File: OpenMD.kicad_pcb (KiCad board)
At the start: 4 copper layers, 80 x 50 mm, 167 parts, among them IC2 RAA211, J1 GND, J2 Digital, J3 Analog, J4 Sensors, J5 A, J6 B, J7 C, J8 V_{BATT}, Q1 EPC2065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

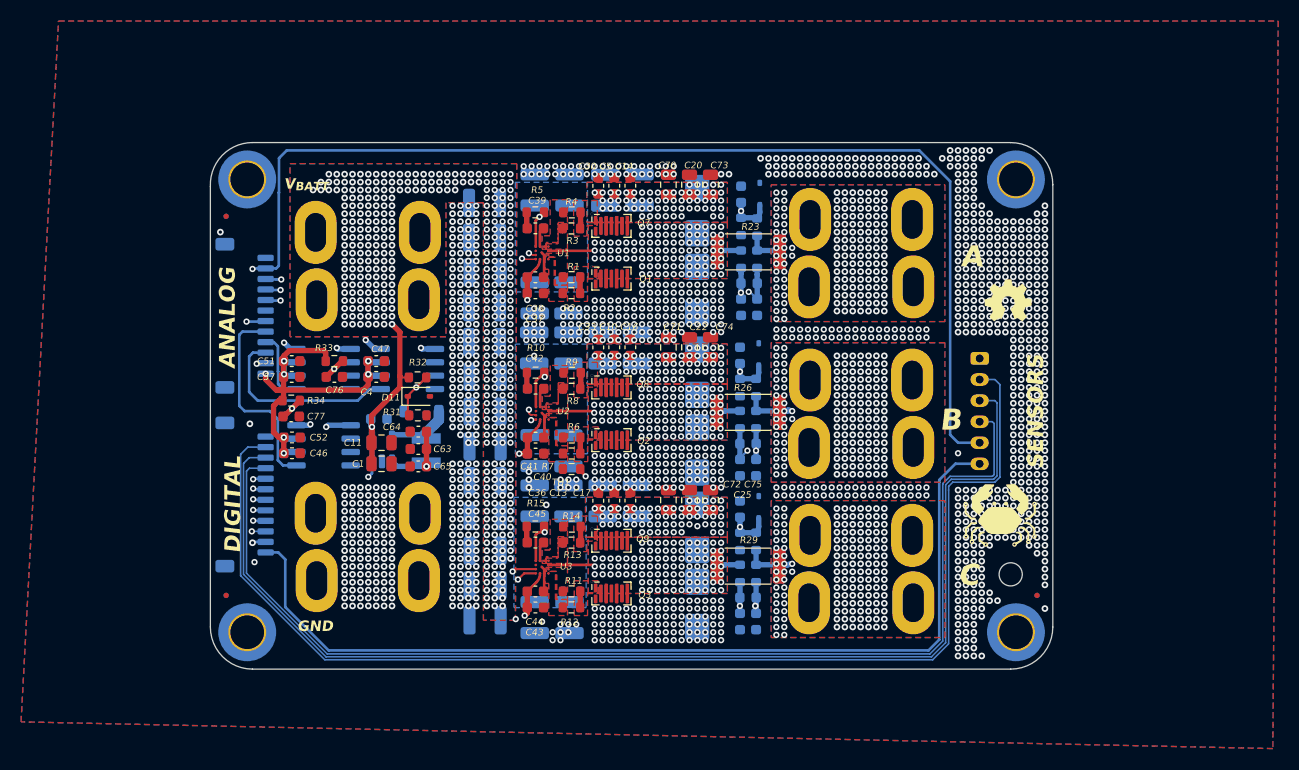
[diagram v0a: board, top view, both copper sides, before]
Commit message: added ESD protection
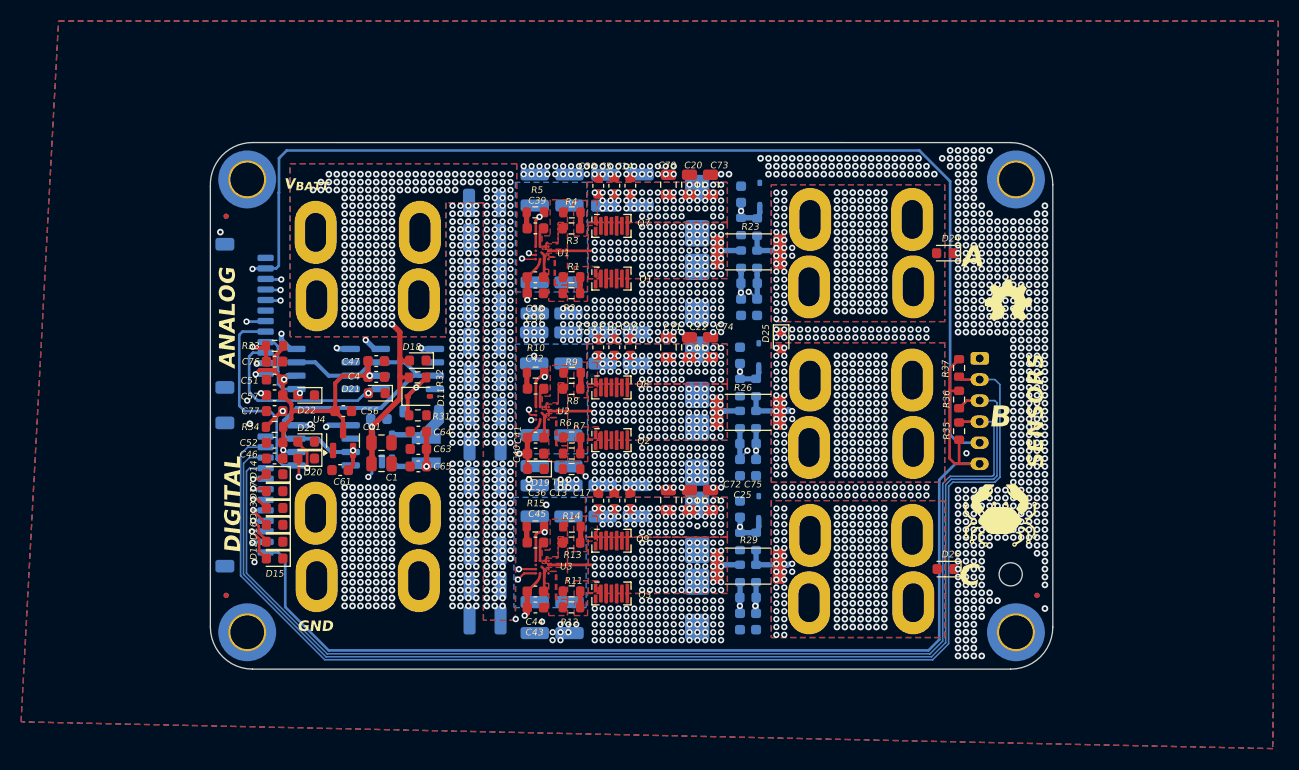
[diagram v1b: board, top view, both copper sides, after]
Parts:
- added C56: 100nF, Capacitor_SMD:C_0603_1608Metric, F.Cu at (110.5, 102.8)
- added C61: 100nF, Capacitor_SMD:C_0603_1608Metric, F.Cu at (110.2, 108.4)
- added D12: 100V, Diode_SMD:D_0603_1608Metric, F.Cu at (104.0, 115.2)
- added D13: 100V, Diode_SMD:D_0603_1608Metric, F.Cu at (104.0, 112.0)
- added D14: 100V, Diode_SMD:D_0603_1608Metric, F.Cu at (104.0, 108.8)
- added D15: 100V, Diode_SMD:D_0603_1608Metric, F.Cu at (104.0, 116.8)
- added D16: 100V, Diode_SMD:D_0603_1608Metric, F.Cu at (104.0, 113.6)
- added D17: 100V, Diode_SMD:D_0603_1608Metric, F.Cu at (104.0, 110.4)
- added D18: 100V, Diode_SMD:D_0603_1608Metric, F.Cu at (117.6, 98.0)
- added D19: 100V, Diode_SMD:D_0603_1608Metric, F.Cu at (128.8, 108.3)
- added D20: 100V, Diode_SMD:D_0603_1608Metric, F.Cu at (107.0, 107.3)
- added D21: 100V, Diode_SMD:D_0603_1608Metric, F.Cu at (113.7, 101.1)
- added D22: 100V, Diode_SMD:D_0603_1608Metric, F.Cu at (107.0, 101.3)
- added D23: 100V, Diode_SMD:D_0603_1608Metric, F.Cu at (107.0, 105.7)
- added D24: 100V, Diode_SMD:D_0603_1608Metric, F.Cu at (167.6, 87.8)
- added D25: 100V, Diode_SMD:D_0603_1608Metric, F.Cu at (152.1, 96.1)
- added D26: 100V, Diode_SMD:D_0603_1608Metric, F.Cu at (167.7, 117.8)
- added R35: 2.2k, Resistor_SMD:R_0603_1608Metric, F.Cu at (169.0, 104.7)
- added R36: 2.2k, Resistor_SMD:R_0603_1608Metric, F.Cu at (169.0, 101.7)
- added R37: 2.2k, Resistor_SMD:R_0603_1608Metric, F.Cu at (169.0, 98.7)
- added U4: LR8103, Package_TO_SOT_SMD:SOT-23, F.Cu at (110.5, 105.6)
- IC2: value RAA211 -> RAA2118054GP3#JA0
- moved C76 5.86 mm to (104.0, 98.1)
- moved R33 5.86 mm to (104.0, 96.6), turned to 180 degrees
- moved R34 2.95 mm to (104.0, 104.3), turned to 180 degrees
- moved C51 2.39 mm to (104.0, 99.8), turned to 180 degrees
- moved C57 2.39 mm to (104.0, 101.3), turned to 180 degrees
- moved C46 1.72 mm to (104.0, 107.3), turned to 180 degrees
- moved C52 1.72 mm to (104.0, 105.8), turned to 180 degrees
- moved C77 1.65 mm to (104.0, 102.8), turned to 180 degrees
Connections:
- U10 pad 3: /GND -> /Phase Current Sensors/REF
- U10 pad 7: /V_{ANA} -> /Phase Current Sensors/REF
- U8 pad 3: /GND -> /Phase Current Sensors/REF
- U8 pad 7: /V_{ANA} -> /Phase Current Sensors/REF
- U9 pad 3: /GND -> /Phase Current Sensors/REF
- U9 pad 7: /V_{ANA} -> /Phase Current Sensors/REF
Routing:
- net /Phase Current Sensors/REF: track 0.00 -> 40.5 mm, vias 0 -> 1
- net /V_{DIG}: track 90.5 -> 106.6 mm
- net /V_{ANA}: track 40.4 -> 33.0 mm, vias 7 -> 4
- net /M_TEMP_SENSE: track 122.2 -> 115.4 mm
- net /I_SENSE.C: track 19.4 -> 23.3 mm, vias 0 -> 1
- net /BATT_SENSE: track 22.3 -> 25.7 mm
- net /INPUT.AL: track 78.9 -> 82.0 mm
- net /INPUT.AH: track 75.2 -> 77.6 mm
- net /HALL.B: track 112.2 -> 114.5 mm
- net /HALL.C: track 116.5 -> 118.2 mm
- net /HALL.A: track 107.9 -> 109.6 mm
- net /ENABLE: track 22.0 -> 23.6 mm, vias 2 -> 3
- net /V_{DRV}: track 60.0 -> 61.4 mm
- net /I_SENSE.A: track 18.4 -> 19.7 mm, vias 0 -> 1
- net /INPUT.BH: track 60.1 -> 61.4 mm
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
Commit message: add context
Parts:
- removed C56, C61: 100nF, Capacitor_SMD:C_0603_1608Metric
- removed U4: LR8103, Package_TO_SOT_SMD:SOT-23
- R23, R26, R29: value 500u -> 300u
- moved C4 0.50 mm to (114.1, 99.6)
- moved C47 0.50 mm to (114.1, 98.1)
- moved D21 0.45 mm to (114.1, 101.1)
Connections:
- U10 pad 3: /Phase Current Sensors/REF -> /GND
- U10 pad 7: /Phase Current Sensors/REF -> /V_{ANA}
- U8 pad 3: /Phase Current Sensors/REF -> /GND
- U8 pad 7: /Phase Current Sensors/REF -> /V_{ANA}
- U9 pad 3: /Phase Current Sensors/REF -> /GND
- U9 pad 7: /Phase Current Sensors/REF -> /V_{ANA}
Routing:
- net /Phase Current Sensors/REF: track 40.5 -> 0.00 mm, vias 1 -> 0
- net /V_{ANA}: track 33.0 -> 42.2 mm
- net /GND: track 6.06 -> 6.80 mm
